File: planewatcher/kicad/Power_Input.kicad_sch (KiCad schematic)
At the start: 8 parts, among them Q1 DMP6023LSS-13

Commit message: work on board layout
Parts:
- renumbered C4 to C68, C19 to C69, D3 to D1, D1 to D2, L4 to L11, R3 to R36
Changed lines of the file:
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@@
 		(dnp no)
 		(fields_autoplaced yes)
-		(property "Reference" "#PWR017"
+		(property "Reference" "#PWR0105"
 			(at 168.91 106.68 0)
 			(hide yes)
@@
 			(project "planewatcher"
 				(path "/7a4a4324-e8b8-4d06-b75a-28095d4e9f10/5ac3603d-bbeb-44f4-b422-6252fe26d95e"
-					(reference "#PWR017")
+					(reference "#PWR0105")
 					(unit 1)
 				)
@@
 		(dnp no)
 		(fields_autoplaced yes)
-		(property "Reference" "L4"
+		(property "Reference" "L11"
 			(at 180.34 83.82 90)
 			(show_name no)
@@
 			(project "planewatcher"
 				(path "/7a4a4324-e8b8-4d06-b75a-28095d4e9f10/5ac3603d-bbeb-44f4-b422-6252fe26d95e"
-					(reference "L4")
+					(reference "L11")
 					(unit 1)
 				)
@@
 		(dnp no)
 		(fields_autoplaced yes)
-		(property "Reference" "D1"
+		(property "Reference" "D2"
 			(at 114.3 95.2499 90)
 			(show_name no)
@@
 			(project "planewatcher"
 				(path "/7a4a4324-e8b8-4d06-b75a-28095d4e9f10/5ac3603d-bbeb-44f4-b422-6252fe26d95e"
-					(reference "D1")
+					(reference "D2")
 					(unit 1)
 				)
@@
 		(dnp no)
 		(fields_autoplaced yes)
-		(property "Reference" "R3"
+		(property "Reference" "R36"
 			(at 139.7 104.1399 0)
 			(show_name no)
@@
 			(project "planewatcher"
 				(path "/7a4a4324-e8b8-4d06-b75a-28095d4e9f10/5ac3603d-bbeb-44f4-b422-6252fe26d95e"
-					(reference "R3")
+					(reference "R36")
 					(unit 1)
 				)
@@
 		(dnp no)
 		(fields_autoplaced yes)
-		(property "Reference" "C4"
+		(property "Reference" "C68"
 			(at 172.72 95.2499 0)
 			(show_name no)
@@
 			(project "planewatcher"
 				(path "/7a4a4324-e8b8-4d06-b75a-28095d4e9f10/5ac3603d-bbeb-44f4-b422-6252fe26d95e"
-					(reference "C4")
+					(reference "C68")
 					(unit 1)
 				)
@@
 		(dnp no)
 		(fields_autoplaced yes)
-		(property "Reference" "C19"
+		(property "Reference" "C69"
 			(at 195.58 95.2499 0)
 			(show_name no)
@@
 			(project "planewatcher"
 				(path "/7a4a4324-e8b8-4d06-b75a-28095d4e9f10/5ac3603d-bbeb-44f4-b422-6252fe26d95e"
-					(reference "C19")
+					(reference "C69")
 					(unit 1)
 				)
@@
 		(dnp no)
 		(fields_autoplaced yes)
-		(property "Reference" "D3"
+		(property "Reference" "D1"
 			(at 148.59 92.7099 90)
 			(show_name no)
@@
 			(project "planewatcher"
 				(path "/7a4a4324-e8b8-4d06-b75a-28095d4e9f10/5ac3603d-bbeb-44f4-b422-6252fe26d95e"
-					(reference "D3")
+					(reference "D1")
 					(unit 1)
 				)
@@
 		(dnp no)
 		(fields_autoplaced yes)
-		(property "Reference" "#PWR043"
+		(property "Reference" "#PWR0106"
 			(at 191.77 106.68 0)
 			(hide yes)
@@
 			(project "planewatcher"
 				(path "/7a4a4324-e8b8-4d06-b75a-28095d4e9f10/5ac3603d-bbeb-44f4-b422-6252fe26d95e"
-					(reference "#PWR043")
+					(reference "#PWR0106")
 					(unit 1)
 				)
@@
 		(dnp no)
 		(fields_autoplaced yes)
-		(property "Reference" "#PWR016"
+		(property "Reference" "#PWR0104"
 			(at 111.76 106.68 0)
 			(hide yes)
@@
 			(project "planewatcher"
 				(path "/7a4a4324-e8b8-4d06-b75a-28095d4e9f10/5ac3603d-bbeb-44f4-b422-6252fe26d95e"
-					(reference "#PWR016")
+					(reference "#PWR0104")
 					(unit 1)
 				)
@@
 		(dnp no)
 		(fields_autoplaced yes)
-		(property "Reference" "#PWR06"
+		(property "Reference" "#PWR0107"
 			(at 137.16 118.11 0)
 			(hide yes)
@@
 			(project "planewatcher"
 				(path "/7a4a4324-e8b8-4d06-b75a-28095d4e9f10/5ac3603d-bbeb-44f4-b422-6252fe26d95e"
-					(reference "#PWR06")
-					(unit 1)
-				)
+					(reference "#PWR0107")
+					(unit 1)
+				)

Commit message: finish first rev pcb
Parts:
- F1: value Polyfuse -> Bourns MF-MSMF200/24X 2.0A; footprint (none) -> Fuse:Fuse_1812_4532Metric
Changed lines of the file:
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@@
 			)
 		)
-		(property "Value" "Polyfuse"
+		(property "Value" "Bourns MF-MSMF200/24X 2.0A"
 			(at 100.33 85.09 90)
 			(show_name no)
@@
 			)
 		)
-		(property "Footprint" ""
+		(property "Footprint" "Fuse:Fuse_1812_4532Metric"
 			(at 105.41 87.63 0)
 			(hide yes)
@@
 			)
 		)
-		(property "Description" "Resettable fuse, polymeric positive temperature coefficient"
+		(property "Description" "2.0A hold resettable PPTC polyfuse, 24V max, 1812, board input overcurrent protection, Bourns MF-MSMF200/24X"
 			(at 100.33 88.9 0)
 			(hide yes)

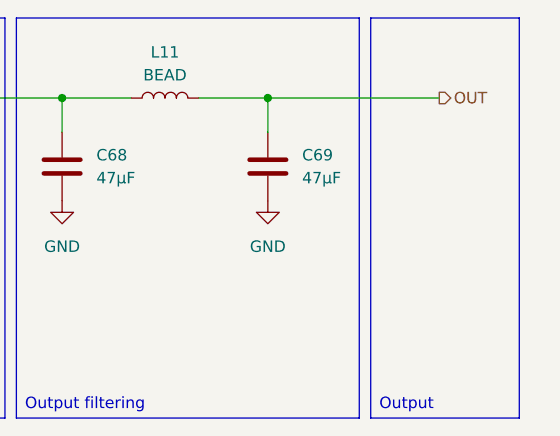
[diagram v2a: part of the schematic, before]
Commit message: add jumpers for testing different power rails & additional test point
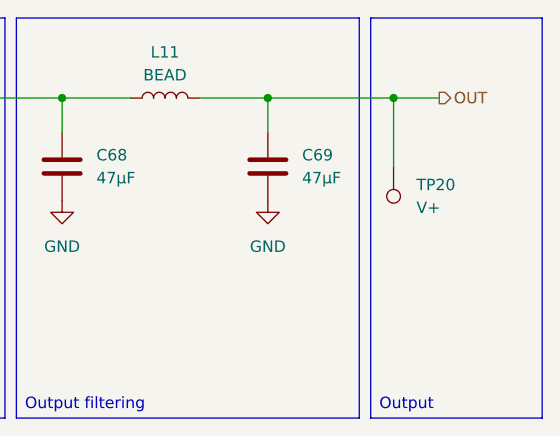
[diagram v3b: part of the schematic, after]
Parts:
- added TP20: V+, TestPoint:TestPoint_Pad_D1.0mm, symbol Connector:TestPoint
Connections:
- net OUT: now also TP20.1
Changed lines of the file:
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@@
 		(exclude_from_sim no)
 		(at 203.2 80.01 0)
-		(size 16.51 44.45)
+		(size 19.05 44.45)
 		(margins 0.9525 0.9525 0.9525 0.9525)
 		(stroke
@@
 	)
 	(junction
+		(at 205.74 88.9)
+		(diameter 0)
+		(color 0 0 0 0)
+	)
+	(junction
 		(at 168.91 88.9)
 		(diameter 0)
@@
 	(wire
 		(pts
+			(xy 205.74 88.9) (xy 210.82 88.9)
+		)
+		(stroke
+			(width 0)
+			(type default)
+		)
+	)
+	(wire
+		(pts
 			(xy 168.91 88.9) (xy 176.53 88.9)
 		)
@@
 	(wire
 		(pts
-			(xy 191.77 88.9) (xy 210.82 88.9)
+			(xy 191.77 88.9) (xy 205.74 88.9)
 		)
 		(stroke
@@
 		(pts
 			(xy 191.77 88.9) (xy 191.77 92.71)
+		)
+		(stroke
+			(width 0)
+			(type default)
+		)
+	)
+	(wire
+		(pts
+			(xy 205.74 96.52) (xy 205.74 88.9)
 		)
 		(stroke
@@
 					(unit 1)
 				)
+			)
+		)
+	)
+	(symbol
+		(lib_id "Connector:TestPoint")
+		(at 205.74 96.52 180)
+		(unit 1)
+		(body_style 1)
+		(exclude_from_sim no)
+		(in_bom yes)
+		(on_board yes)
+		(in_pos_files yes)
+		(dnp no)
+		(fields_autoplaced yes)
+		(property "Reference" "TP20"
+			(at 208.28 98.5519 0)
+			(show_name no)
+			(do_not_autoplace no)
+			(effects
+				(font
+					(size 1.27 1.27)
+				)
+				(justify right)
+			)
+		)
+		(property "Value" "V+"
+			(at 208.28 101.0919 0)
+			(show_name no)
+			(do_not_autoplace no)
+			(effects
+				(font
+					(size 1.27 1.27)
+				)
+				(justify right)
+			)
+		)
+		(property "Footprint" "TestPoint:TestPoint_Pad_D1.0mm"
+			(at 200.66 96.52 0)
+			(hide yes)
+			(show_name no)
+			(do_not_autoplace no)
+			(effects
+				(font
+					(size 1.27 1.27)
+				)
+			)
+		)
+		(property "Datasheet" ""
+			(at 200.66 96.52 0)
+			(hide yes)
+			(show_name no)
+			(do_not_autoplace no)
+			(effects
+				(font
+					(size 1.27 1.27)
+				)
+			)
+		)
+		(property "Description" "test point"
+			(at 205.74 96.52 0)
+			(hide yes)
+			(show_name no)
+			(do_not_autoplace no)
+			(effects
+				(font
+					(size 1.27 1.27)
+				)
+			)
+		)
+		(pin "1"
+		)
+		(instances
+			(project "planewatcher"
+				(path "/7a4a4324-e8b8-4d06-b75a-28095d4e9f10/5ac3603d-bbeb-44f4-b422-6252fe26d95e"
+					(reference "TP20")
+					(unit 1)
+				)

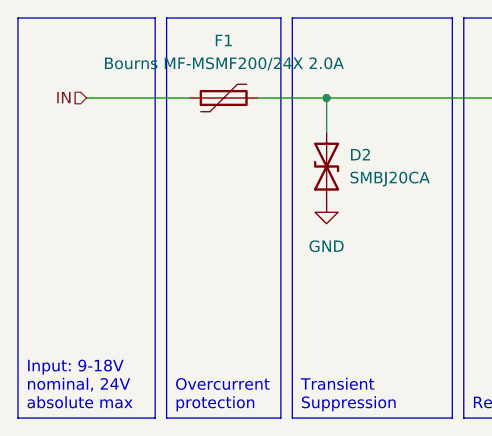
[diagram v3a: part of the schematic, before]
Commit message: address & fix ERC errors/warnings
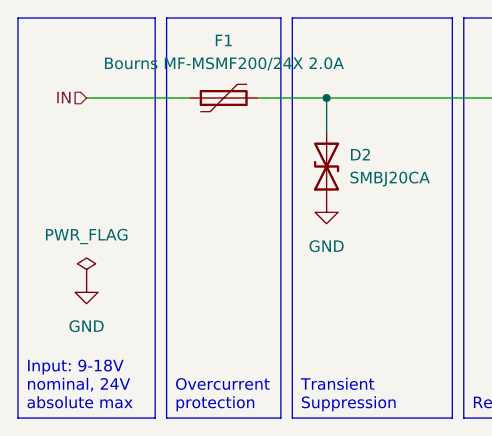
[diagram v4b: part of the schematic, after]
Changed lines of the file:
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@@
+	(symbol
+		(lib_id "power:GND")
+		(at 85.09 109.22 0)
+		(unit 1)
+		(body_style 1)
+		(exclude_from_sim no)
+		(in_bom yes)
+		(on_board yes)
+		(in_pos_files yes)
+		(dnp no)
+		(fields_autoplaced yes)
+		(property "Reference" "#PWR07"
+			(at 85.09 115.57 0)
+			(hide yes)
+			(show_name no)
+			(do_not_autoplace no)
+			(effects
+				(font
+					(size 1.27 1.27)
+				)
+			)
+		)
+		(property "Value" "GND"
+			(at 85.09 114.3 0)
+			(show_name no)
+			(do_not_autoplace no)
+			(effects
+				(font
+					(size 1.27 1.27)
+				)
+			)
+		)
+		(property "Footprint" ""
+			(at 85.09 109.22 0)
+			(hide yes)
+			(show_name no)
+			(do_not_autoplace no)
+			(effects
+				(font
+					(size 1.27 1.27)
+				)
+			)
+		)
+		(property "Datasheet" ""
+			(at 85.09 109.22 0)
+			(hide yes)
+			(show_name no)
+			(do_not_autoplace no)
+			(effects
+				(font
+					(size 1.27 1.27)
+				)
+			)
+		)
+		(property "Description" "Power symbol creates a global label with name \"GND\" , ground"
+			(at 85.09 109.22 0)
+			(hide yes)
+			(show_name no)
+			(do_not_autoplace no)
+			(effects
+				(font
+					(size 1.27 1.27)
+				)
+			)
+		)
+		(pin "1"
+		)
+		(instances
+			(project "planewatcher"
+				(path "/7a4a4324-e8b8-4d06-b75a-28095d4e9f10/5ac3603d-bbeb-44f4-b422-6252fe26d95e"
+					(reference "#PWR07")
+					(unit 1)
+				)
+			)
+		)
+	)
 	(symbol
 		(lib_id "power:GND")
@@
 					(unit 1)
 				)
+			)
+		)
+	)
+	(symbol
+		(lib_id "power:PWR_FLAG")
+		(at 85.09 109.22 0)
+		(unit 1)
+		(body_style 1)
+		(exclude_from_sim no)
+		(in_bom yes)
+		(on_board yes)
+		(in_pos_files yes)
+		(dnp no)
+		(fields_autoplaced yes)
+		(property "Reference" "#FLG011"
+			(at 85.09 107.315 0)
+			(hide yes)
+			(show_name no)
+			(do_not_autoplace no)
+			(effects
+				(font
+					(size 1.27 1.27)
+				)
+			)
+		)
+		(property "Value" "PWR_FLAG"
+			(at 85.09 104.14 0)
+			(show_name no)
+			(do_not_autoplace no)
+			(effects
+				(font
+					(size 1.27 1.27)
+				)
+			)
+		)
+		(property "Footprint" ""
+			(at 85.09 109.22 0)
+			(hide yes)
+			(show_name no)
+			(do_not_autoplace no)
+			(effects
+				(font
+					(size 1.27 1.27)
+				)
+			)
+		)
+		(property "Datasheet" ""
+			(at 85.09 109.22 0)
+			(hide yes)
+			(show_name no)
+			(do_not_autoplace no)
+			(effects
+				(font
+					(size 1.27 1.27)
+				)
+			)
+		)
+		(property "Description" "Special symbol for telling ERC where power comes from"
+			(at 85.09 109.22 0)
+			(hide yes)
+			(show_name no)
+			(do_not_autoplace no)
+			(effects
+				(font
+					(size 1.27 1.27)
+				)
+			)
+		)
+		(pin "1"
+		)
+		(instances
+			(project "planewatcher"
+				(path "/7a4a4324-e8b8-4d06-b75a-28095d4e9f10/5ac3603d-bbeb-44f4-b422-6252fe26d95e"
+					(reference "#FLG011")
+					(unit 1)
+				)

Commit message: updates before fab
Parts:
- C68, C69: Purpose (none) -> Input bulk capacitance for board power after protection and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; Suggested Part (none) -> Taiyo Yuden TMK325ABJ476MM-P
- D1: Purpose (none) -> Limits P-channel MOSFET gate-source voltage during reverse/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; Suggested Part (none) -> Diodes Inc. BZT52C12-7-F
- D2: Purpose (none) -> Clamps input supply transients on the protected power input.; Suggested Part (none) -> Littelfuse SMBJ20CA
- F1: value Bourns MF-MSMF200/24X 2.0A -> Littelfuse 1812L300/24SLER 3.0A; Purpose (none) -> Provides resettable overcurrent protection at the board pow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; Suggested Part (none) -> Littelfuse 1812L300/24SLER
- L11: Purpose (none) -> Filters conducted noise on the protected board input supply.; Suggested Part (none) -> Murata BLM31PG601SN1L
- Q1: Purpose (none) -> Implements low-loss reverse-polarity protection on the boar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; Suggested Part (none) -> Diodes Inc. DMP6023LSS-13
- R36: Purpose (none) -> Gate bias/pull resistor for the input reverse-polarity P-ch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; Suggested Part (none) -> Yageo RC0603FR-07100KL
- TP20: Purpose (none) -> Provides oscilloscope/DMM probe access to V+.; Suggested Part (none) -> No fitted part (PCB pad only); now left out of the parts list

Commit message: rationalise power to single 3V3 rail fed from FPGA VCC
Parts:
- removed C68, C69: 47µF, Capacitor_SMD:C_1210_3225Metric, symbol Device:C
- removed D1: 12V, Diode_SMD:D_SOD-123F, symbol Device:D_Zener_Filled
- removed L11: BEAD, Inductor_SMD:L_1206_3216Metric, symbol Device:L
- removed Q1: DMP6023LSS-13, planewatcher:Q_DMP6023LSS, symbol Transistor_FET:Q_PMOS_DGS
- removed R36: 100kΩ, Resistor_SMD:R_0603_1608Metric, symbol Device:R
- D2: value SMBJ20CA -> TPD1E10B06; footprint Diode_SMD:D_SMB -> Diode_SMD:D_SOD-523; Suggested Part Littelfuse SMBJ20CA -> Texas Instruments TPD1E10B06DYAR
- F1: value Littelfuse 1812L300/24SLER 3.0A -> Littelfuse 1812L110/24DR 1.1A; Suggested Part Littelfuse 1812L300/24SLER -> Littelfuse 1812L110/24DR
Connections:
- net OUT: now also D2.2 (A2), F1.2
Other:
- moved on the sheet: TP20
